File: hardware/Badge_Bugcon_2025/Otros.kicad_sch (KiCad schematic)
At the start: 9 parts, among them J7 Add_On, J9 Add_On

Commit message: feat(Hw):Update_Schematic_And_Route
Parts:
- renumbered C33 to C2, D10 to D7, R46 to R4
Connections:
- net PB2: now reaches C37.2, SW5.2
- net PB1: now reaches C43.2, SW7.2
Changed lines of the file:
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@@
+		)
+	)
+	(hierarchical_label "PB1"
+		(shape output)
+		(at 157.48 44.45 180)
+		(effects
+			(font
+				(size 1.27 1.27)
+			)
+			(justify right)
 		)
 	)
@@
 			)
 			(justify left)
+		)
+	)
+	(hierarchical_label "PB2"
+		(shape output)
+		(at 156.21 63.5 180)
+		(effects
+			(font
+				(size 1.27 1.27)
+			)
+			(justify right)
 		)
 	)
@@
 		(on_board yes)
 		(dnp no)
-		(property "Reference" "D10"
+		(property "Reference" "D7"
 			(at 45.212 107.188 0)
 			(effects
@@
 			(project "Badge_Bugcon_2025"
 				(path "/a95785a0-0aa1-454e-b59f-0ac64970ac71/2ee5046e-0e56-46eb-b0bb-bea5e503cbc9"
-					(reference "D10")
+					(reference "D7")
 					(unit 1)
 				)
@@
 		(dnp no)
 		(fields_autoplaced yes)
-		(property "Reference" "R46"
+		(property "Reference" "R4"
 			(at 39.37 105.41 90)
 			(effects
@@
 			(project "Badge_Bugcon_2025"
 				(path "/a95785a0-0aa1-454e-b59f-0ac64970ac71/2ee5046e-0e56-46eb-b0bb-bea5e503cbc9"
-					(reference "R46")
+					(reference "R4")
 					(unit 1)
 				)
@@
 		(on_board yes)
 		(dnp no)
-		(property "Reference" "C33"
+		(property "Reference" "C2"
 			(at 54.61 98.552 0)
 			(effects
@@
 			(project "Badge_Bugcon_2025"
 				(path "/a95785a0-0aa1-454e-b59f-0ac64970ac71/2ee5046e-0e56-46eb-b0bb-bea5e503cbc9"
-					(reference "C33")
+					(reference "C2")
 					(unit 1)
 				)

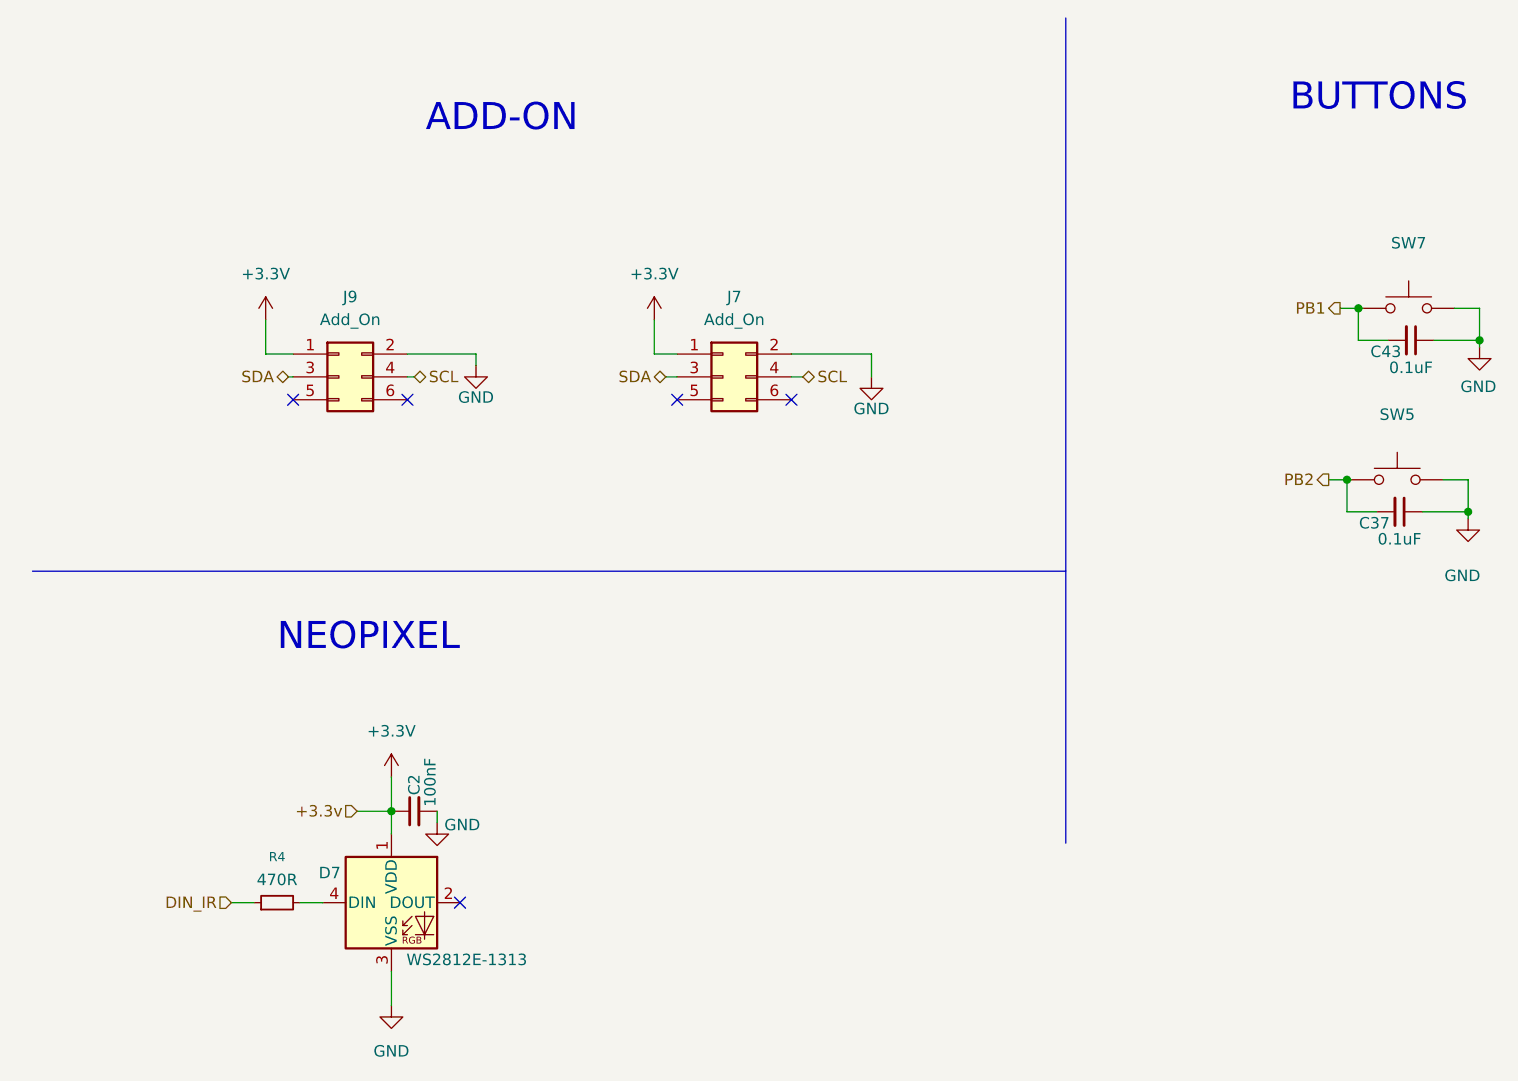
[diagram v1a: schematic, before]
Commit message: feat(Hw): Add leds change crytsla routing
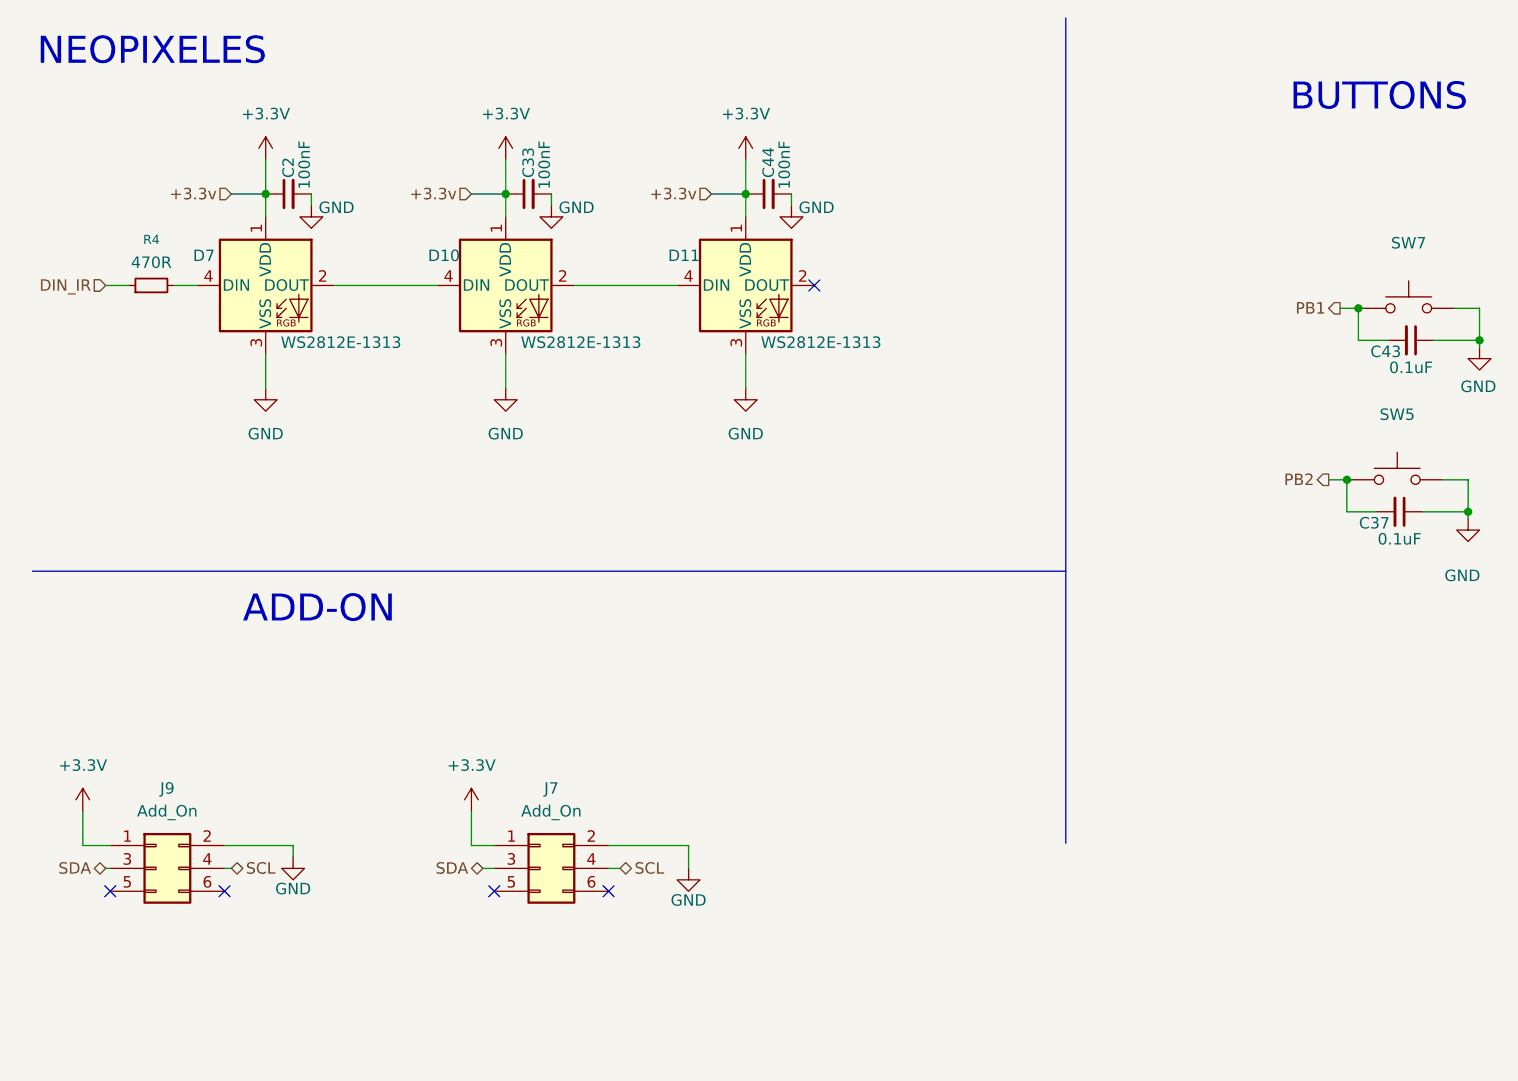
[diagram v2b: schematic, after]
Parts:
- added C33, C44: 100nF, Capacitor_SMD:C_0402_1005Metric, symbol Device:C_Small
- added D10, D11: WS2812E-1313, Footprints:WS2812E-1313, symbol LED:WS2812B
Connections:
- net +3.3V: now also C33.1, C44.1, D10.1 (VDD), D11.1 (VDD)
- net GND: now also C33.2, C44.2, D10.3 (VSS), D11.3 (VSS)
- net at D7.2 (DOUT): now also D10.4 (DIN)
- new net: D10.2 (DOUT), D11.4 (DIN)
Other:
- note added: "NEOPIXELES"
- note removed: "NEOPIXEL"
- moved on the sheet: C2, D7, J7, J9, R4
